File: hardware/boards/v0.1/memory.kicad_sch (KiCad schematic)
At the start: 17 parts, among them IC1 W25Q512JVEIQ, IC4 IS42S16160J-7TLI, J3 MICRO_SD, U22 XTSDG08GWSIGA

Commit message: feat: change charger, fuel gauge, and battery connector, re-route power system
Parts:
- R13, R14, R15, R16, R17: JLC C25531 -> C25744
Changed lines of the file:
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@@
 			)
 		)
-		(property "JLC" "C25531"
+		(property "JLC" "C25744"
 			(at 207.01 109.22 0)
 			(effects
@@
 			)
 		)
-		(property "JLC" "C25531"
+		(property "JLC" "C25744"
 			(at 191.77 109.22 0)
 			(effects
@@
 			)
 		)
-		(property "JLC" "C25531"
+		(property "JLC" "C25744"
 			(at 214.63 109.22 0)
 			(effects
@@
 			)
 		)
-		(property "JLC" "C25531"
+		(property "JLC" "C25744"
 			(at 199.39 109.22 0)
 			(effects
@@
 			)
 		)
-		(property "JLC" "C25531"
+		(property "JLC" "C25744"
 			(at 222.25 109.22 0)
 			(effects

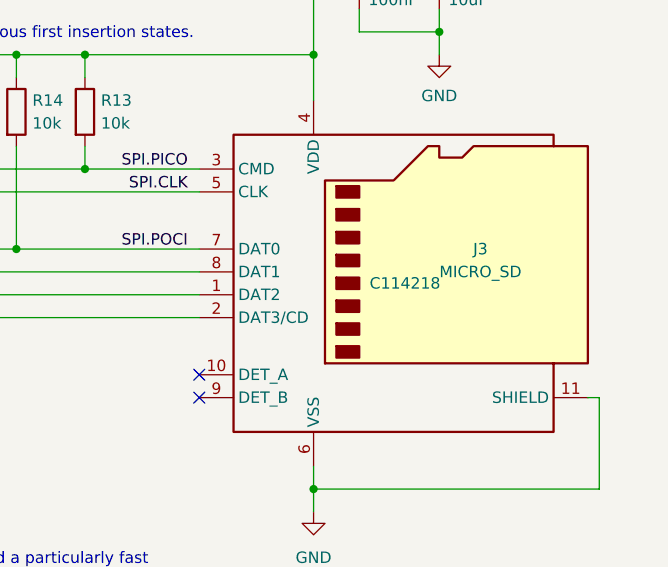
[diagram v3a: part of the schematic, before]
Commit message: feat: various layout and routing adjustments
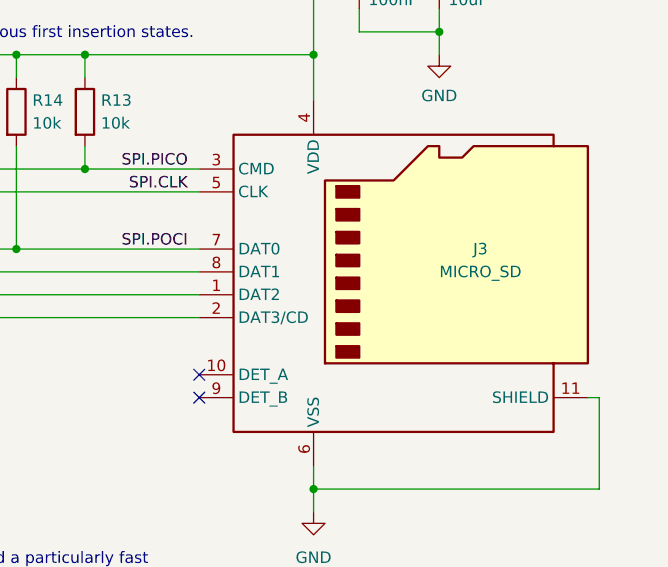
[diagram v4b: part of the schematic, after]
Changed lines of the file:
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@@
+		(polyline
+			(pts
+				(xy 121.92 81.28) (xy 121.92 101.6) (xy 134.62 101.6) (xy 134.62 81.28)
+			)
+			(stroke
+				(width 0)
+				(type dash)
+			)
+			(fill
+				(type none)
+			)
+		)
+	)
+	(rule_area
 		(polyline
 			(pts
 				(xy 121.92 81.28) (xy 121.92 59.69) (xy 134.62 59.69) (xy 134.62 81.28)
-			)
-			(stroke
-				(width 0)
-				(type dash)
-			)
-			(fill
-				(type none)
-			)
-		)
-	)
-	(rule_area
-		(polyline
-			(pts
-				(xy 121.92 81.28) (xy 121.92 101.6) (xy 134.62 101.6) (xy 134.62 81.28)
 			)
 			(stroke
@@
 			)
 		)
-		(property "Characteristics " ""
-			(at 207.01 109.22 0)
-			(effects
-				(font
-					(size 1.27 1.27)
-				)
-			)
-		)
 		(property "Sim.Enable" ""
 			(at 207.01 109.22 0)
@@
 			)
 		)
-		(property "Characteristics " ""
-			(at 252.73 93.98 0)
-			(effects
-				(font
-					(size 1.27 1.27)
-				)
-			)
-		)
 		(property "Sim.Enable" ""
 			(at 252.73 93.98 0)
@@
 			)
 		)
-		(property "Characteristics " ""
-			(at 269.24 48.26 0)
-			(effects
-				(font
-					(size 1.27 1.27)
-				)
-			)
-		)
 		(property "Sim.Enable" ""
 			(at 269.24 48.26 0)
@@
 			)
 		)
-		(property "Characteristics " ""
-			(at 160.02 187.96 0)
-			(effects
-				(font
-					(size 1.27 1.27)
-				)
-			)
-		)
 		(property "Sim.Enable" ""
 			(at 160.02 187.96 0)
@@
 			)
 		)
-		(property "Characteristics " ""
-			(at 160.02 193.04 0)
-			(effects
-				(font
-					(size 1.27 1.27)
-				)
-			)
-		)
 		(property "Sim.Enable" ""
 			(at 160.02 193.04 0)
@@
 			)
 		)
-		(property "Characteristics " ""
-			(at 191.77 109.22 0)
-			(effects
-				(font
-					(size 1.27 1.27)
-				)
-			)
-		)
 		(property "Sim.Enable" ""
 			(at 191.77 109.22 0)
@@
 			)
 		)
-		(property "Characteristics " ""
-			(at 160.02 172.72 0)
-			(effects
-				(font
-					(size 1.27 1.27)
-				)
-			)
-		)
 		(property "Sim.Enable" ""
 			(at 160.02 172.72 0)
@@
 			)
 		)
-		(property "Characteristics " ""
-			(at 160.02 177.8 0)
-			(effects
-				(font
-					(size 1.27 1.27)
-				)
-			)
-		)
 		(property "Sim.Enable" ""
 			(at 160.02 177.8 0)
@@
 			)
 		)
-		(property "Characteristics " ""
-			(at 214.63 109.22 0)
-			(effects
-				(font
-					(size 1.27 1.27)
-				)
-			)
-		)
 		(property "Sim.Enable" ""
 			(at 214.63 109.22 0)
@@
 			)
 		)
-		(property "Characteristics " ""
-			(at 199.39 109.22 0)
-			(effects
-				(font
-					(size 1.27 1.27)
-				)
-			)
-		)
 		(property "Sim.Enable" ""
 			(at 199.39 109.22 0)
@@
 			)
 		)
-		(property "Characteristics " ""
-			(at 160.02 182.88 0)
-			(effects
-				(font
-					(size 1.27 1.27)
-				)
-			)
-		)
 		(property "Sim.Enable" ""
 			(at 160.02 182.88 0)
@@
 			)
 		)
-		(property "Characteristics " ""
-			(at 210.82 50.8 0)
-			(effects
-				(font
-					(size 1.27 1.27)
-				)
-			)
-		)
 		(property "Sim.Enable" ""
 			(at 210.82 50.8 0)
@@
 			)
 		)
-		(property "Characteristics " ""
-			(at 105.41 93.98 0)
-			(effects
-				(font
-					(size 1.27 1.27)
-				)
-			)
-		)
 		(property "Sim.Enable" ""
 			(at 105.41 93.98 0)
@@
 			)
 		)
-		(property "Characteristics " ""
-			(at 261.62 93.98 0)
-			(effects
-				(font
-					(size 1.27 1.27)
-				)
-			)
-		)
 		(property "Sim.Enable" ""
 			(at 261.62 93.98 0)
@@
 			)
 		)
-		(property "Characteristics " ""
-			(at 214.63 27.94 0)
-			(effects
-				(font
-					(size 1.27 1.27)
-				)
-			)
-		)
 		(property "Sim.Enable" ""
 			(at 214.63 27.94 0)
@@
 			)
 		)
-		(property "Characteristics " ""
-			(at 222.25 109.22 0)
-			(effects
-				(font
-					(size 1.27 1.27)
-				)
-			)
-		)
 		(property "Sim.Enable" ""
 			(at 222.25 109.22 0)
@@
 					(size 1.27 1.27)
 				)
+				(hide yes)
 			)
 		)
@@
 			(at 257.81 128.27 0)
 			(effects
-				(font
-					(size 1.27 1.27)
-				)
-			)
-		)
-		(property "Characteristics " ""
-			(at 257.81 128.27 0)
-			(effects

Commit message: feat: add pins in silkscreen, various DFM adjustments for JLC
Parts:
- IC4: FT Rotation Offset (none) -> -90
- J3: FT Position Offset (none) -> 0,0.1905
- U22: FT Rotation Offset (none) -> 180

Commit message: chore: remove unused symbol attributes
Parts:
- IC1: Height 0.8 -> (none)
- IC4: Height 1.2 -> (none)
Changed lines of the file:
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@@
-			)
-		)
-		(property "Sim.Enable" ""
-			(at 207.01 109.22 0)
-			(effects
-				(font
-					(size 1.27 1.27)
-				)
 			)
 		)
@@
 				)
 				(hide yes)
-			)
-		)
-		(property "Sim.Enable" ""
-			(at 252.73 93.98 0)
-			(effects
-				(font
-					(size 1.27 1.27)
-				)
 			)
 		)
@@
 			)
 		)
-		(property "Height" "0.8"
-			(at 288.29 436.83 0)
-			(effects
-				(font
-					(size 1.27 1.27)
-				)
-				(justify left top)
-				(hide yes)
-			)
-		)
 		(property "JLC" "C2986165"
 			(at 269.24 48.26 0)
@@
 				)
 				(hide yes)
-			)
-		)
-		(property "Sim.Enable" ""
-			(at 269.24 48.26 0)
-			(effects
-				(font
-					(size 1.27 1.27)
-				)
 			)
 		)
@@
 			)
 		)
-		(property "Sim.Enable" ""
-			(at 160.02 187.96 0)
-			(effects
-				(font
-					(size 1.27 1.27)
-				)
-			)
-		)
 		(pin "1"
 		)
@@
 			)
 		)
-		(property "Sim.Enable" ""
-			(at 160.02 193.04 0)
-			(effects
-				(font
-					(size 1.27 1.27)
-				)
-			)
-		)
 		(pin "1"
 		)
@@
 				)
 				(hide yes)
-			)
-		)
-		(property "Sim.Enable" ""
-			(at 191.77 109.22 0)
-			(effects
-				(font
-					(size 1.27 1.27)
-				)
 			)
 		)
@@
 			)
 		)
-		(property "Sim.Enable" ""
-			(at 160.02 172.72 0)
-			(effects
-				(font
-					(size 1.27 1.27)
-				)
-			)
-		)
 		(pin "1"
 		)
@@
 			)
 		)
-		(property "Sim.Enable" ""
-			(at 160.02 177.8 0)
-			(effects
-				(font
-					(size 1.27 1.27)
-				)
-			)
-		)
 		(pin "1"
 		)
@@
 			)
 		)
-		(property "Sim.Enable" ""
-			(at 214.63 109.22 0)
-			(effects
-				(font
-					(size 1.27 1.27)
-				)
-			)
-		)
 		(pin "1"
 		)
@@
 				)
 				(hide yes)
-			)
-		)
-		(property "Sim.Enable" ""
-			(at 199.39 109.22 0)
-			(effects
-				(font
-					(size 1.27 1.27)
-				)
 			)
 		)
@@
 			)
 		)
-		(property "Sim.Enable" ""
-			(at 160.02 182.88 0)
-			(effects
-				(font
-					(size 1.27 1.27)
-				)
-			)
-		)
 		(pin "1"
 		)
@@
 			)
 		)
-		(property "Sim.Enable" ""
-			(at 210.82 50.8 0)
-			(effects
-				(font
-					(size 1.27 1.27)
-				)
-			)
-		)
 		(pin "1"
 		)
@@
 			)
 		)
-		(property "Height" "1.2"
-			(at 118.11 458.42 0)
-			(effects
-				(font
-					(size 1.27 1.27)
-				)
-				(justify left top)
-				(hide yes)
-			)
-		)
 		(property "JLC" "C412833"
 			(at 105.41 93.98 0)
@@
 			)
 		)
-		(property "Sim.Enable" ""
-			(at 105.41 93.98 0)
-			(effects
-				(font
-					(size 1.27 1.27)
-				)
-			)
-		)
 		(pin "49"
 		)
@@
 			)
 		)
-		(property "Sim.Enable" ""
-			(at 261.62 93.98 0)
-			(effects
-				(font
-					(size 1.27 1.27)
-				)
-			)
-		)
 		(pin "2"
 		)
@@
 				)
 				(hide yes)
-			)
-		)
-		(property "Sim.Enable" ""
-			(at 214.63 27.94 0)
-			(effects
-				(font
-					(size 1.27 1.27)
-				)
 			)
 		)
@@
 			)
 		)
-		(property "Sim.Enable" ""
-			(at 222.25 109.22 0)
-			(effects
-				(font
-					(size 1.27 1.27)
-				)
-			)
-		)

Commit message: fix: rotation offsets and LEDs on wrong side of board
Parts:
- U22: FT Rotation Offset 180 -> -90
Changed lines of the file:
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@@
 			)
 		)
-		(property "FT Rotation Offset" "180"
+		(property "FT Rotation Offset" "-90"
 			(at 210.82 50.8 0)
 			(effects

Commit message: chore: more DFM tweaks
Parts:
- added TP56: QCLK, TestPoint:TestPoint_Pad_D1.0mm, symbol Connector:TestPoint
- added TP57: QIO3, TestPoint:TestPoint_Pad_D1.0mm, symbol Connector:TestPoint
- added TP58: QIO2, TestPoint:TestPoint_Pad_D1.0mm, symbol Connector:TestPoint
- added TP59: QIO1, TestPoint:TestPoint_Pad_D1.0mm, symbol Connector:TestPoint
- added TP60: QIO0, TestPoint:TestPoint_Pad_D1.0mm, symbol Connector:TestPoint
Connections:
- net QSPI.CLK: now also TP56.1
- net QSPI.IO0: now also TP60.1
- net QSPI.IO1: now also TP59.1
- net QSPI.IO2: now also TP58.1
- net QSPI.IO3: now also TP57.1
